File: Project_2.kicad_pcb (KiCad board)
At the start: 4 copper layers, 88.9 x 63.5 mm, 117 parts, among them CON3 BARREL_JACK, J1 USB, P1 CONN_01X10, P2 CONN_01X02, Q1 RTQ020N03, Q2 RTQ020N03, Q3 RTQ020N03, Q4 RTQ020N03, Q5 RTQ020N03, U1 LM2675_Adj, U2 LM2675_5V, U3 SM72442, U4 SM72295, U5 TLV2371_DBV

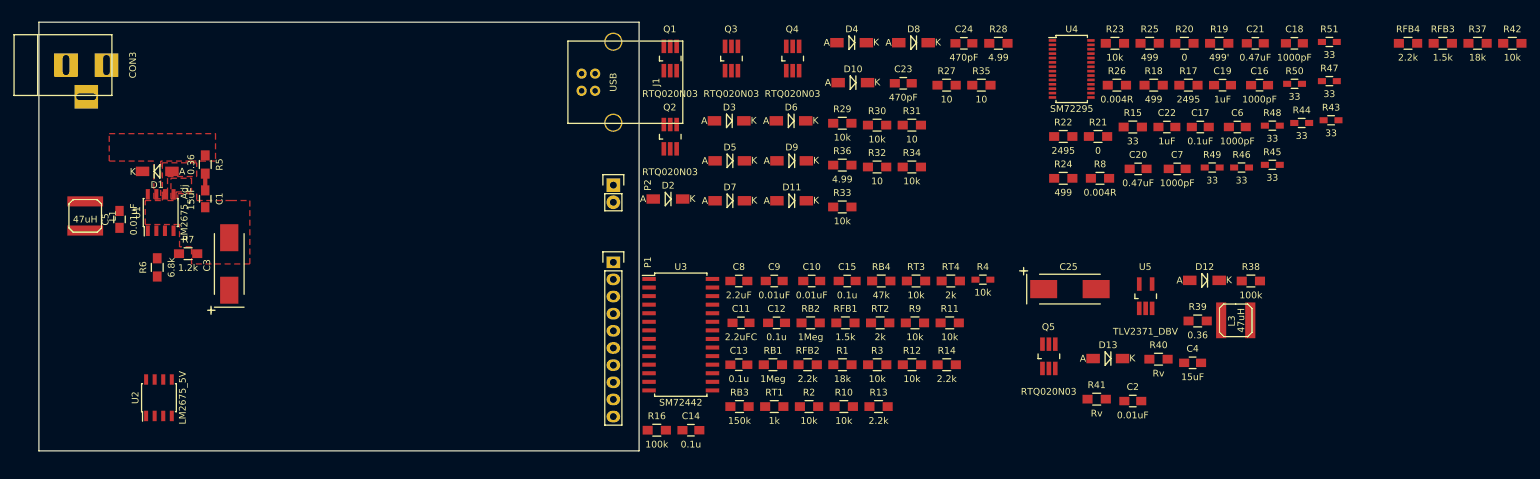
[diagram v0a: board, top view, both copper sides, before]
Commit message: still trying to get initial placements done.  Still need to fine-tune
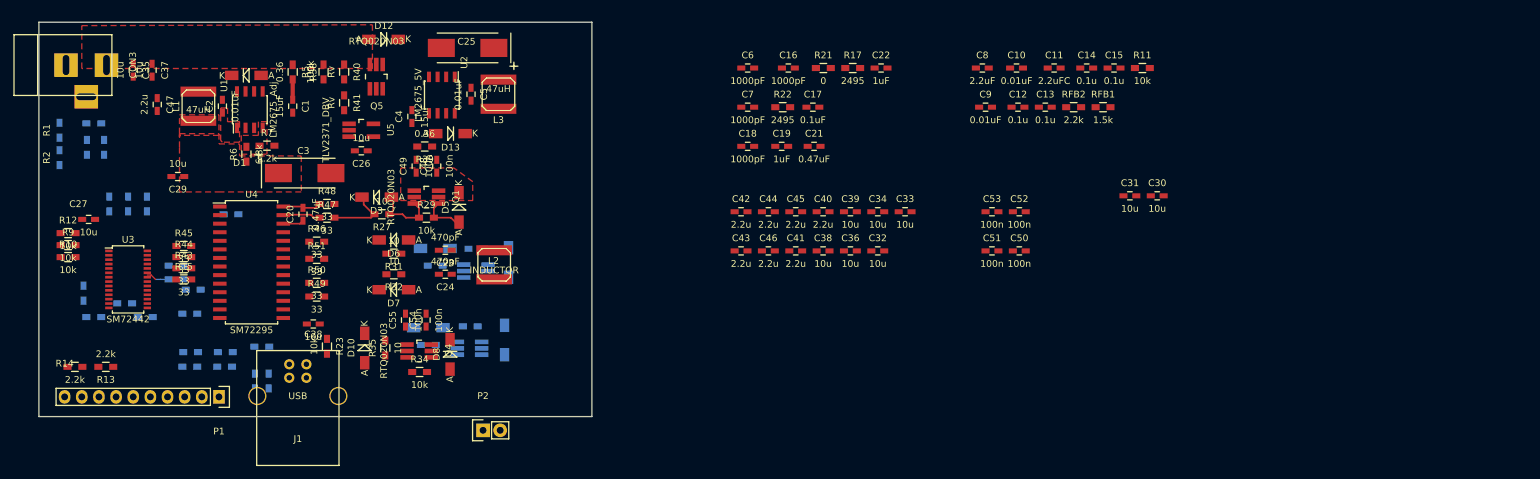
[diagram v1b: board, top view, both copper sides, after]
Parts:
- added C26: 10u, Capacitors_SMD:C_0603_HandSoldering, F.Cu at (103.6, 101.6)
- added C27: 10u, Capacitors_SMD:C_0603_HandSoldering, F.Cu at (63.2, 111.8)
- added C28: 10u, Capacitors_SMD:C_0603_HandSoldering, F.Cu at (96.5, 127.3)
- added C29: 10u, Capacitors_SMD:C_0603_HandSoldering, F.Cu at (76.5, 105.4)
- added C30: 10u, Capacitors_SMD:C_0603_HandSoldering, F.Cu at (221.5, 108.3)
- added C31: 10u, Capacitors_SMD:C_0603_HandSoldering, F.Cu at (217.5, 108.3)
- added C32: 10u, Capacitors_SMD:C_0603_HandSoldering, F.Cu at (180.1, 116.4)
- added C33: 10u, Capacitors_SMD:C_0603_HandSoldering, F.Cu at (184.2, 110.6)
- added C34: 10u, Capacitors_SMD:C_0603_HandSoldering, F.Cu at (180.1, 110.6)
- added C35: 10u, Capacitors_SMD:C_0603_HandSoldering, F.Cu at (69.8, 89.7)
- added C36: 10u, Capacitors_SMD:C_0603_HandSoldering, F.Cu at (176.1, 116.4)
- added C37: 10u, Capacitors_SMD:C_0603_HandSoldering, F.Cu at (72.6, 89.7)
- added C38: 10u, Capacitors_SMD:C_0603_HandSoldering, F.Cu at (172.0, 116.4)
- added C39: 10u, Capacitors_SMD:C_0603_HandSoldering, F.Cu at (176.1, 110.6)
- added C40: 2.2u, Capacitors_SMD:C_0603_HandSoldering, F.Cu at (172.0, 110.6)
- added C41: 2.2u, Capacitors_SMD:C_0603_HandSoldering, F.Cu at (168.0, 116.4)
- added C42: 2.2u, Capacitors_SMD:C_0603_HandSoldering, F.Cu at (159.9, 110.6)
- added C43: 2.2u, Capacitors_SMD:C_0603_HandSoldering, F.Cu at (159.9, 116.4)
- added C44: 2.2u, Capacitors_SMD:C_0603_HandSoldering, F.Cu at (163.9, 110.6)
- added C45: 2.2u, Capacitors_SMD:C_0603_HandSoldering, F.Cu at (168.0, 110.6)
- added C46: 2.2u, Capacitors_SMD:C_0603_HandSoldering, F.Cu at (163.9, 116.4)
- added C47: 2.2u, Capacitors_SMD:C_0603_HandSoldering, F.Cu at (73.4, 94.7)
- added C48: 100n, Capacitors_SMD:C_0603_HandSoldering, F.Cu at (114.8, 103.9)
- added C49: 100n, Capacitors_SMD:C_0603_HandSoldering, F.Cu at (111.8, 103.9)
- added C50: 100n, Capacitors_SMD:C_0603_HandSoldering, F.Cu at (201.1, 116.4)
- added C51: 100n, Capacitors_SMD:C_0603_HandSoldering, F.Cu at (197.1, 116.4)
- added C52: 100n, Capacitors_SMD:C_0603_HandSoldering, F.Cu at (201.1, 110.6)
- added C53: 100n, Capacitors_SMD:C_0603_HandSoldering, F.Cu at (197.1, 110.6)
- added C54: 100n, Capacitors_SMD:C_0603_HandSoldering, F.Cu at (113.2, 126.7)
- added C55: 100n, Capacitors_SMD:C_0603_HandSoldering, F.Cu at (110.2, 126.7)
- added L2: INDUCTOR, Inductors:SELF-WE-TPC_M, F.Cu at (123.3, 118.5)
- C1, C10, C11, C12, C13, C14, C15, C16, C17, C18, C19, C2, C20, C21, C22, C23, C24, C4, C5, C6, C7, C8, C9: footprint Capacitors_SMD:C_0805_HandSoldering -> Capacitors_SMD:C_0603_HandSoldering
- D11, D2, D4, D9, Q2, Q3, R4: moved to B.Cu
- R1, R16, R18, R19, R2, R20, R24, R25, R26, R28, R3, R30, R33, R36, R37, R42, R8, RB1, RB2, RB3, RB4, RFB3, RFB4, RT1, RT2, RT3, RT4: footprint Resistors_SMD:R_0805_HandSoldering -> Resistors_SMD:R_0603_HandSoldering; moved to B.Cu
- R10, R11, R12, R13, R14, R15, R17, R21, R22, R23, R27, R29, R31, R32, R34, R35, R38, R39, R40, R41, R5, R6, R7, R9, RFB1, RFB2: footprint Resistors_SMD:R_0805_HandSoldering -> Resistors_SMD:R_0603_HandSoldering
- U3: footprint Housings_SOIC:SOIC-28_7.5x17.9mm_Pitch1.27mm -> Housings_SSOP:TSSOP-28_4.4x9.7mm_Pitch0.65mm
- U4: footprint Housings_SSOP:TSSOP-28_4.4x9.7mm_Pitch0.65mm -> Housings_SOIC:SOIC-28_7.5x17.9mm_Pitch1.27mm
- moved R42 196.7 mm to (83.4, 133.6)
- moved R37 196.7 mm to (78.2, 133.6)
- moved RFB4 186.1 mm to (78.3, 131.4)
- moved RFB3 186.1 mm to (83.5, 131.4)
- moved R43 171.4 mm to (77.3, 119.0)
- moved R19 168.4 mm to (63.0, 101.1), turned to 270 degrees
- moved R44 166.8 mm to (77.3, 117.3)
- moved R45 161.7 mm to (77.3, 115.7)
- moved R18 155.7 mm to (65.5, 101.1), turned to 270 degrees
- moved R51 153.4 mm to (97.0, 117.6)
- moved R47 149.9 mm to (98.6, 111.5)
- moved R8 149.3 mm to (64.0, 97.5)
- moved R50 147.8 mm to (97.0, 121.2)
- moved R20 143.5 mm to (84.3, 111.0)
- moved R15 142.4 mm to (77.3, 120.7)
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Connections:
- P2 pad 1: Vout_D -> Vbatt
- R25 pad 2: Vout_D -> Vbatt
- R26 pad 2: Vout_D -> Vbatt
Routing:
- net Net-(D3-Pad1): track 0.00 -> 9.78 mm
- net /HBridge/HOA: track 0.00 -> 9.42 mm
- net /HBridge/HSA: track 0.00 -> 6.34 mm
- net Net-(C20-Pad2): track 0.00 -> 5.69 mm
- net Net-(R47-Pad1): track 0.00 -> 5.58 mm
- net Net-(C20-Pad1): track 0.00 -> 3.11 mm
- net (no net): track 0.00 -> 1.48 mm
- net Net-(C14-Pad1): track 0.00 -> 1.44 mm
- added copper zone on F.Cu, net 8VDC
- added copper zone on In1.Cu, net GNDD
- added copper zone on F.Cu, net Net-(C2-Pad1)
- added copper zone on F.Cu, net Net-(R6-Pad2)
- added copper zone on F.Cu, net Vin
- removed copper zone on F.Cu, net GNDD
- removed copper zone on F.Cu, net Net-(U1-Pad5)
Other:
- board size 88.9 x 63.5 mm -> 81.9 x 58.4 mm

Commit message: Started routing and dicing up power planes
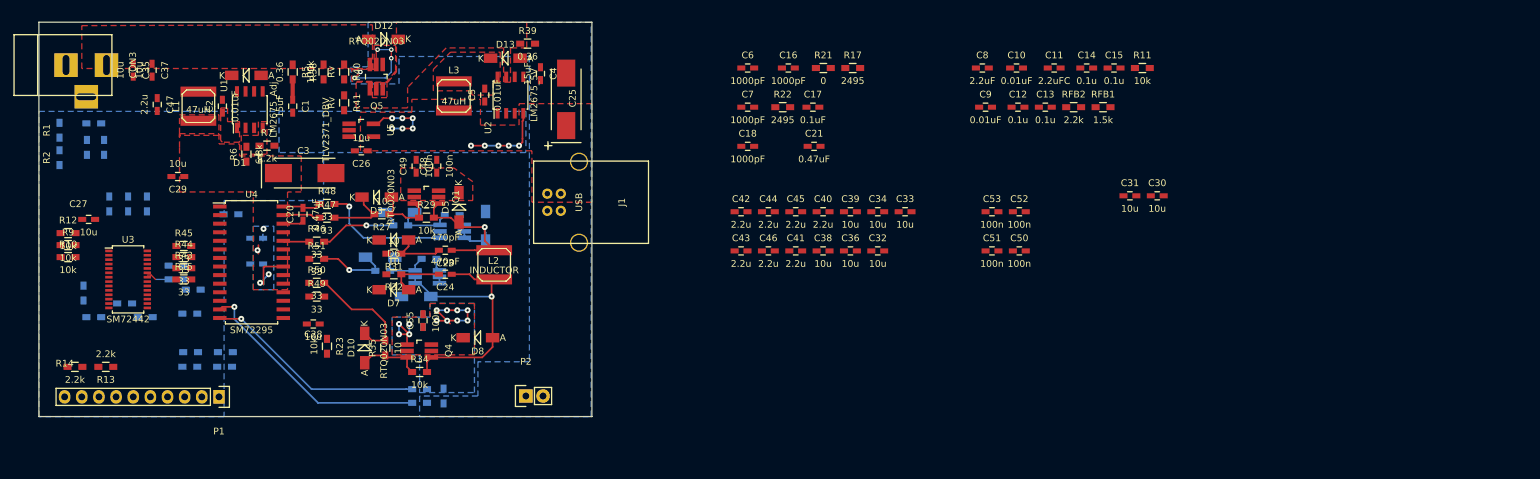
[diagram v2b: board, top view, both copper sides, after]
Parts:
- C19, C22, C54: moved to B.Cu
- moved C22 95.9 mm to (88.1, 114.6), turned to 180 degrees
- moved C19 79.7 mm to (88.1, 118.4), turned to 180 degrees
- moved J1 50.6 mm to (135.9, 109.2), turned to 90 degrees
- moved R26 27.9 mm to (115.8, 137.9), turned to 270 degrees
- moved R24 24.4 mm to (112.3, 136.9), turned to 0 degrees
- moved R25 22.6 mm to (112.3, 138.9), turned to 0 degrees
- moved R39 21.6 mm to (128.3, 85.7), turned to 0 degrees
- moved C4 20.1 mm to (130.2, 90.2), turned to 270 degrees
- moved C25 16.5 mm to (134.0, 94.0), turned to 90 degrees
- moved D9 14.6 mm to (111.8, 123.2), turned to 0 degrees
- moved D13 13.8 mm to (125.0, 87.9), turned to 180 degrees
- moved R36 12.9 mm to (106.8, 119.4)
- moved D11 12.7 mm to (106.4, 117.3)
- moved Q3 12.3 mm to (113.4, 120.3)
- moved R33 11.7 mm to (113.7, 117.6)
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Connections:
- C48 pad 1: Net-(C48-Pad1) -> Vin
- C48 pad 2: Net-(C48-Pad2) -> GNDD
- C49 pad 1: Net-(C49-Pad1) -> Vin
- C49 pad 2: Net-(C49-Pad2) -> GNDD
- C50 pad 1: Net-(C50-Pad1) -> /HBridge/HSA
- C50 pad 2: Net-(C50-Pad2) -> GNDD
- C51 pad 1: Net-(C51-Pad1) -> /HBridge/HSA
- C51 pad 2: Net-(C51-Pad2) -> GNDD
- C52 pad 1: Net-(C52-Pad1) -> /HBridge/HSB
- C52 pad 2: Net-(C52-Pad2) -> GNDD
- C53 pad 1: Net-(C53-Pad1) -> /HBridge/HSB
- C53 pad 2: Net-(C53-Pad2) -> GNDD
- C54 pad 1: Net-(C54-Pad1) -> Vout
- C54 pad 2: Net-(C54-Pad2) -> GNDD
- C55 pad 1: Net-(C55-Pad1) -> Vout
- C55 pad 2: Net-(C55-Pad2) -> GNDD
- R12 pad 1: +5VD -> 5VDC
- R13 pad 1: +5VD -> 5VDC
- R14 pad 1: +5VD -> 5VDC
- R9 pad 1: +5VD -> 5VDC
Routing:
- net /HBridge/HSB: track 0.00 -> 43.5 mm, vias 0 -> 1
- net /HBridge/HSA: track 6.34 -> 47.1 mm, vias 0 -> 2
- net Net-(R25-Pad1): track 0.00 -> 35.6 mm, vias 0 -> 1
- net Net-(R24-Pad1): track 0.00 -> 32.9 mm, vias 0 -> 1
- net 5VDC: track 0.00 -> 22.9 mm, vias 0 -> 11
- net Vout: track 0.00 -> 21.6 mm, vias 0 -> 12
- net /HBridge/HOB: track 0.00 -> 17.7 mm
- net Vbatt: track 0.00 -> 14.7 mm, vias 0 -> 5
- net /HBridge/LOA: track 0.00 -> 13.7 mm, vias 0 -> 1
- net /HBridge/LOB: track 0.00 -> 11.0 mm, vias 0 -> 1
- net 8VDC: track 0.00 -> 9.56 mm, vias 0 -> 4
- net Net-(D10-Pad1): track 0.00 -> 9.34 mm
- net Net-(D2-Pad1): track 0.00 -> 8.80 mm
- net Net-(C24-Pad2): track 0.00 -> 8.30 mm
- net Net-(C23-Pad2): track 0.00 -> 8.26 mm
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- added copper zone on B.Cu, net 5VDC
- added copper zone on F.Cu, net 5VDC
- added copper zone on B.Cu, net 8VDC
- added copper zone on F.Cu, net Net-(C5-Pad2)
- added copper zone on F.Cu, net Net-(D12-Pad2)
- added copper zone on B.Cu, net Vbatt
- added copper zone on F.Cu, net Vbatt
- added copper zone on B.Cu, net Vout
- added copper zone on F.Cu, net Vout
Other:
- net class Default: via_dia 0.889 -> 0.6858; via_drill 0.635 -> 0.3302

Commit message: Routing done, prepping for DRC
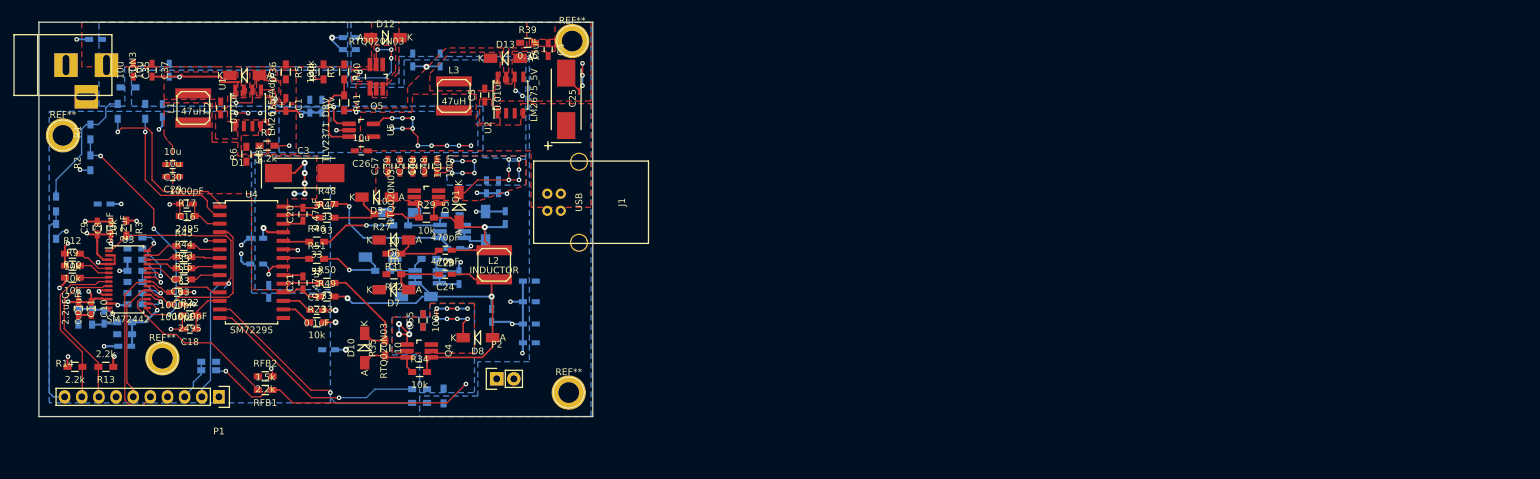
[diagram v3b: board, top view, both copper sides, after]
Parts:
- removed R20, R21: 0, Resistors_SMD:R_0603_HandSoldering
- added C56: 10u, Capacitors_SMD:C_0603_HandSoldering, F.Cu at (111.3, 103.9)
- added C57: 10u, Capacitors_SMD:C_0603_HandSoldering, F.Cu at (107.6, 103.9)
- added C58: 2.2u, Capacitors_SMD:C_0603_HandSoldering, B.Cu at (96.0, 95.0)
- added C59: 2.2u, Capacitors_SMD:C_0603_HandSoldering, B.Cu at (74.2, 95.6)
- added REF**: 1pin, Connect:1pin, F.Cu at (74.2, 132.3)
- added REF**: 1pin, Connect:1pin, F.Cu at (59.4, 99.3)
- added REF**: 1pin, Connect:1pin, F.Cu at (134.4, 137.4)
- added REF**: 1pin, Connect:1pin, F.Cu at (134.9, 85.3)
- C12, C13, C14, C15, C27, C28, C31, C32, C33, C34, C36, C38, C40, C41, C42, C43, C44, C45, C46, C47, C50, C51, C52, C53, R11: moved to B.Cu
- R3: moved to F.Cu
- moved R11 151.9 mm to (70.1, 117.7)
- moved C11 148.9 mm to (61.7, 125.0), turned to 270 degrees
- moved C30 145.9 mm to (75.7, 103.6), turned to 180 degrees
- moved C15 142.7 mm to (76.3, 122.6)
- moved C10 141.6 mm to (63.6, 125.0), turned to 270 degrees
- moved C13 140.9 mm to (68.6, 130.6), turned to 180 degrees
- moved C14 139.2 mm to (76.3, 124.3)
- moved C12 138.9 mm to (65.5, 126.2), turned to 270 degrees
- moved C9 132.8 mm to (64.5, 113.0), turned to 90 degrees
- moved C8 131.2 mm to (66.5, 113.0), turned to 90 degrees
- moved RFB1 131.0 mm to (89.4, 137.0), turned to 180 degrees
- moved C31 128.4 mm to (89.9, 122.4), turned to 270 degrees
- moved RFB2 126.2 mm to (89.4, 135.0)
- moved R17 101.0 mm to (77.9, 111.3)
- moved R22 93.1 mm to (78.2, 126.0)
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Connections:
- C33 pad 1: Vin_D -> Vin
- C39 pad 1: Vin_D -> Vin
- C41 pad 1: Vin_D -> Vin
- C45 pad 1: Vin_D -> Vin
- C6 pad 1: /MPPT/BIN_OUT -> /Connectors/BIN_OUT
- C7 pad 1: /MPPT/BOUT_OUT -> /Connectors/BOUT_OUT
- P1 pad 1: /Connectors/RST -> GNDD
- P1 pad 10: GNDD -> Net-(P1-Pad10)
- P1 pad 2: Net-(P1-Pad2) -> /Connectors/RST
- P1 pad 4: GNDD -> 5VDC
- P1 pad 5: /Connectors/BOUT -> /Connectors/BOUT_OUT
- P1 pad 6: /Connectors/BIN -> /Connectors/BIN_OUT
- R37 pad 2: Net-(P1-Pad3) -> Net-(P1-Pad10)
- R42 pad 1: Net-(P1-Pad3) -> Net-(P1-Pad10)
- RFB3 pad 2: Net-(P1-Pad2) -> Net-(P1-Pad3)
- RFB4 pad 1: Net-(P1-Pad2) -> Net-(P1-Pad3)
- U3 pad 19: /MPPT/BIN_OUT -> /Connectors/BIN_OUT
- U3 pad 21: /MPPT/BOUT_OUT -> /Connectors/BOUT_OUT
- U4 pad 11: /Connectors/BOUT -> /Connectors/BOUT_OUT
- U4 pad 4: /Connectors/BIN -> /Connectors/BIN_OUT
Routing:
- net GNDD: track 3.66 -> 162.6 mm, vias 0 -> 48
- net /Connectors/RST: track 0.00 -> 48.3 mm, vias 0 -> 1
- net /Connectors/BIN_OUT: track 0.00 -> 42.7 mm
- net Vout: track 21.6 -> 63.0 mm, vias 12 -> 14
- net Net-(R1-Pad2): track 0.00 -> 36.3 mm, vias 0 -> 3
- net /Connectors/BOUT_OUT: track 0.00 -> 36.2 mm
- net 5VDC: track 22.9 -> 54.5 mm, vias 11 -> 20
- net Net-(P1-Pad10): track 0.00 -> 30.3 mm
- net Vin: track 0.00 -> 28.6 mm, vias 0 -> 12
- net Net-(R19-Pad2): track 0.00 -> 26.4 mm, vias 0 -> 1
- net Net-(RFB1-Pad2): track 0.00 -> 25.3 mm
- net /Connectors/SCL_I2C: track 0.00 -> 24.5 mm
- net /Connectors/SDA_I2C: track 0.00 -> 24.0 mm
- net Net-(R18-Pad2): track 0.00 -> 22.8 mm, vias 0 -> 1
- net Vin_D: track 0.00 -> 20.0 mm
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- added copper zone on F.Cu, net GNDD
- added copper zone on In2.Cu, net GNDD
- added copper zone on F.Cu, net Net-(C1-Pad1)
- added copper zone on F.Cu, net Net-(C2-Pad2)
- added copper zone on F.Cu, net Net-(C4-Pad1)
- added copper zone on F.Cu, net Net-(C5-Pad1)
- added copper zone on F.Cu, net Net-(U1-Pad5)
- added copper zone on B.Cu, net Vin
- added copper zone on B.Cu, net Vin_D
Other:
- board size 81.9 x 58.4 mm -> 82 x 58.4 mm

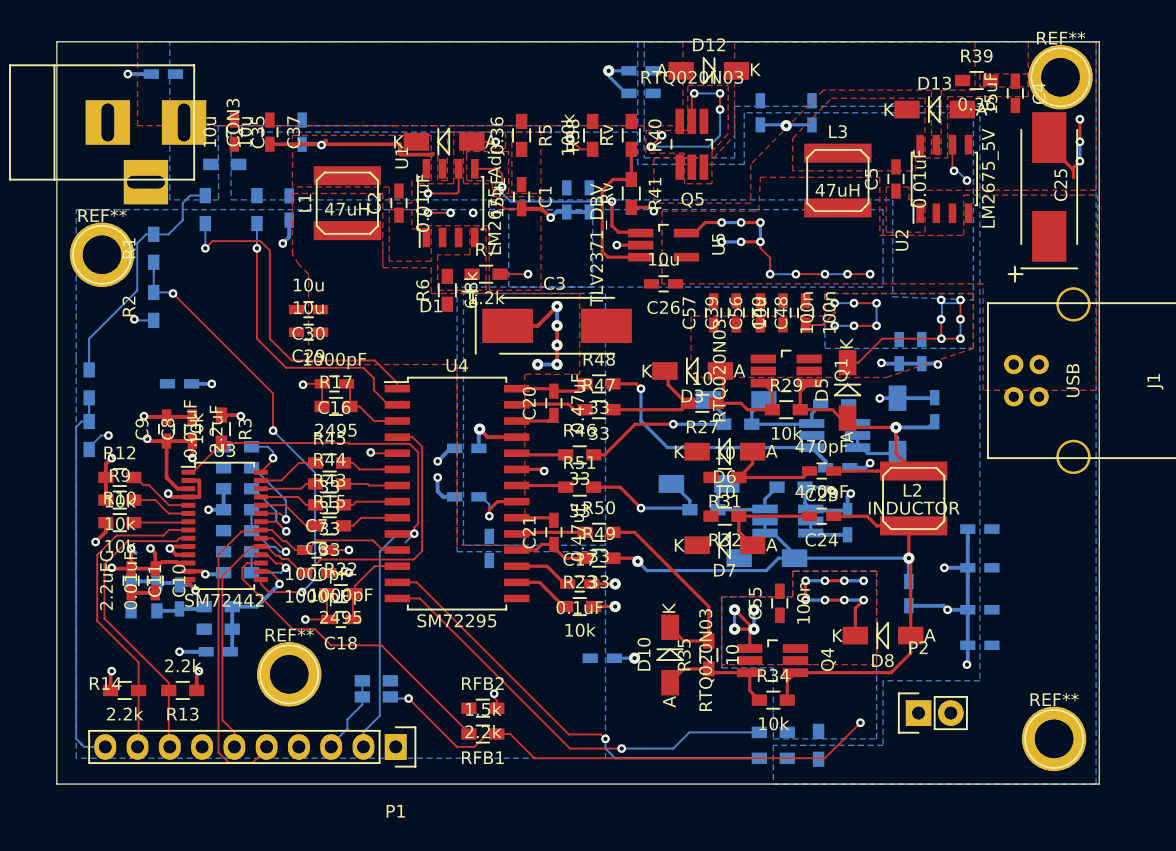
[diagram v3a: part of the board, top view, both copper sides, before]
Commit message: Cleared clearance errors. still chasing down connection issues
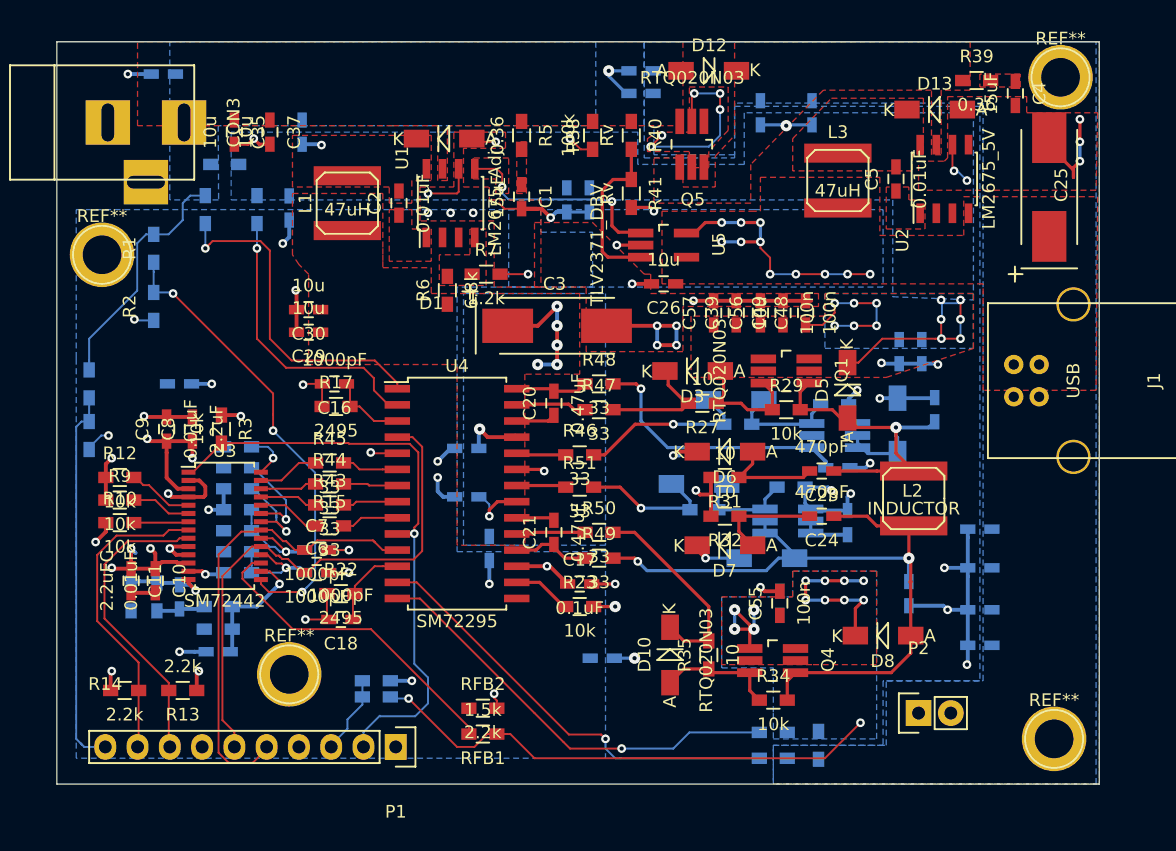
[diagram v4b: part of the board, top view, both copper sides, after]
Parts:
- moved D1 0.25 mm to (86.4, 90.2)
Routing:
- net GNDD: track 162.6 -> 193.8 mm, vias 48 -> 63
- net (no net): track 2.69 -> 0.72 mm
- net Net-(C14-Pad1): track 6.92 -> 8.54 mm
- net Net-(C15-Pad1): track 7.73 -> 9.25 mm
- net 5VDC: track 54.5 -> 54.7 mm, vias 20 -> 21
